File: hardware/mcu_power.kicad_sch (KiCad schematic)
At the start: 85 parts, among them Q201 MMBT3904, Q202 IRLML2244, SW201 Button Power, SW202 Reset, SW203 Button Enter, SW204 Button Left, SW205 Button Up, SW206 Button Down, SW207 Button Escape, SW208 Button Right, U201 STM32F405RGTx, U202 TPS7A2033, U203 TP6841S6, Y201 8 MHz

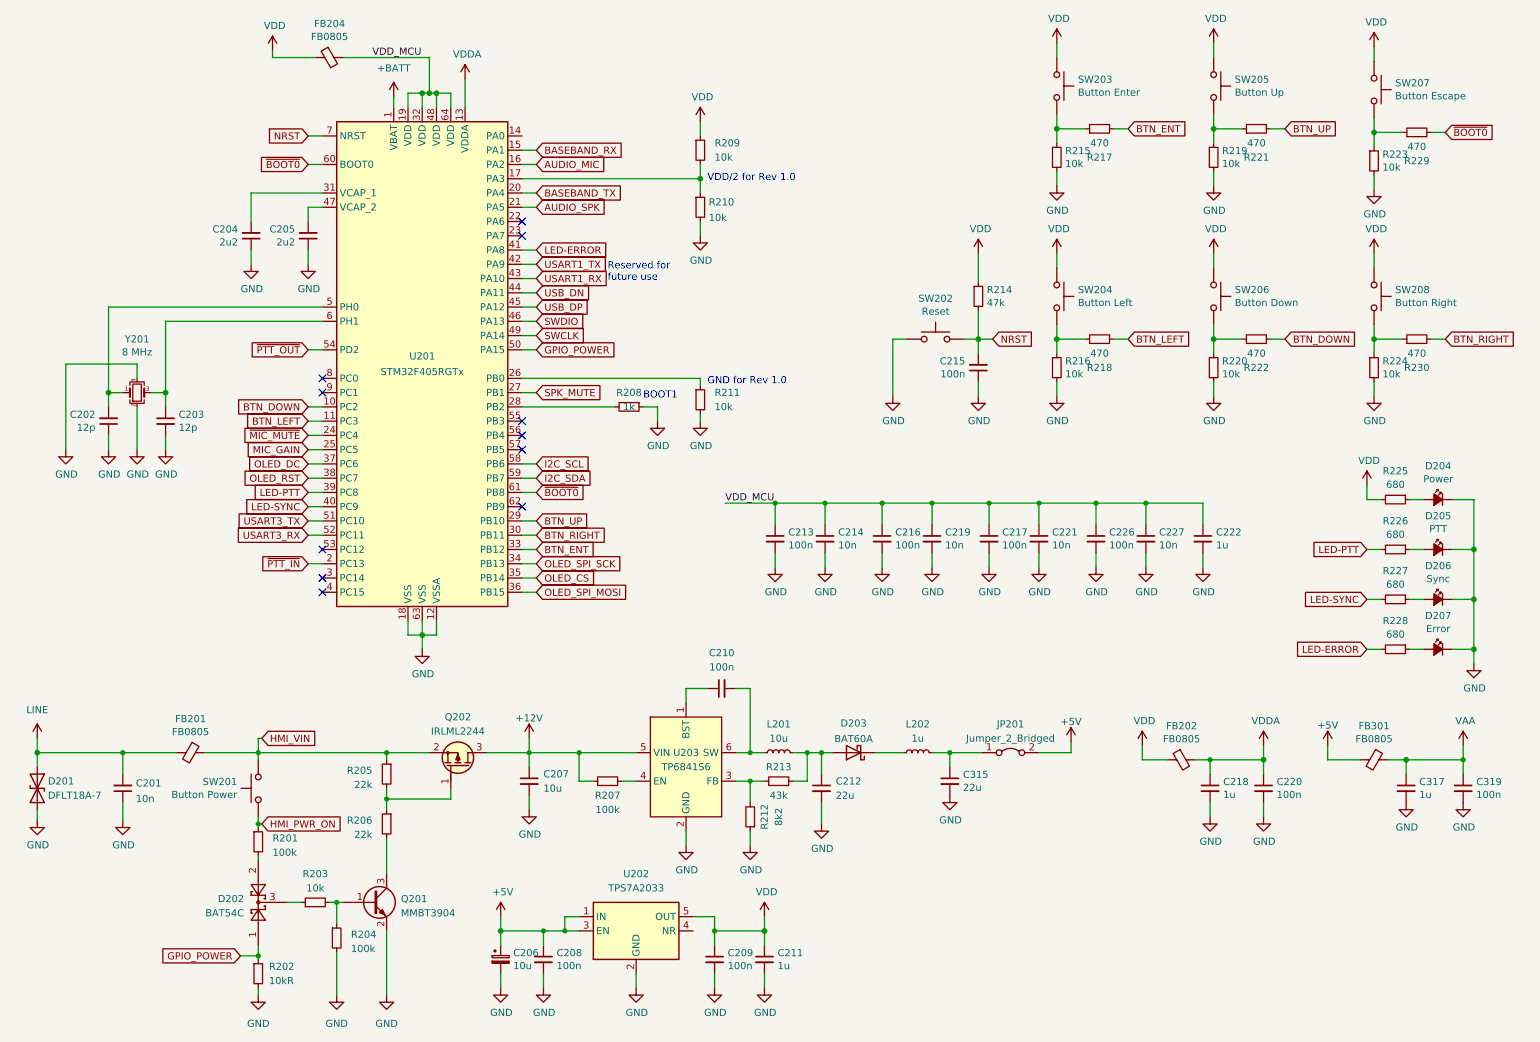
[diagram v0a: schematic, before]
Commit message: Updated various symbols attributes
Updated various components (mostly LEDs and switches) to simplify the BOM and make it more easily readable.
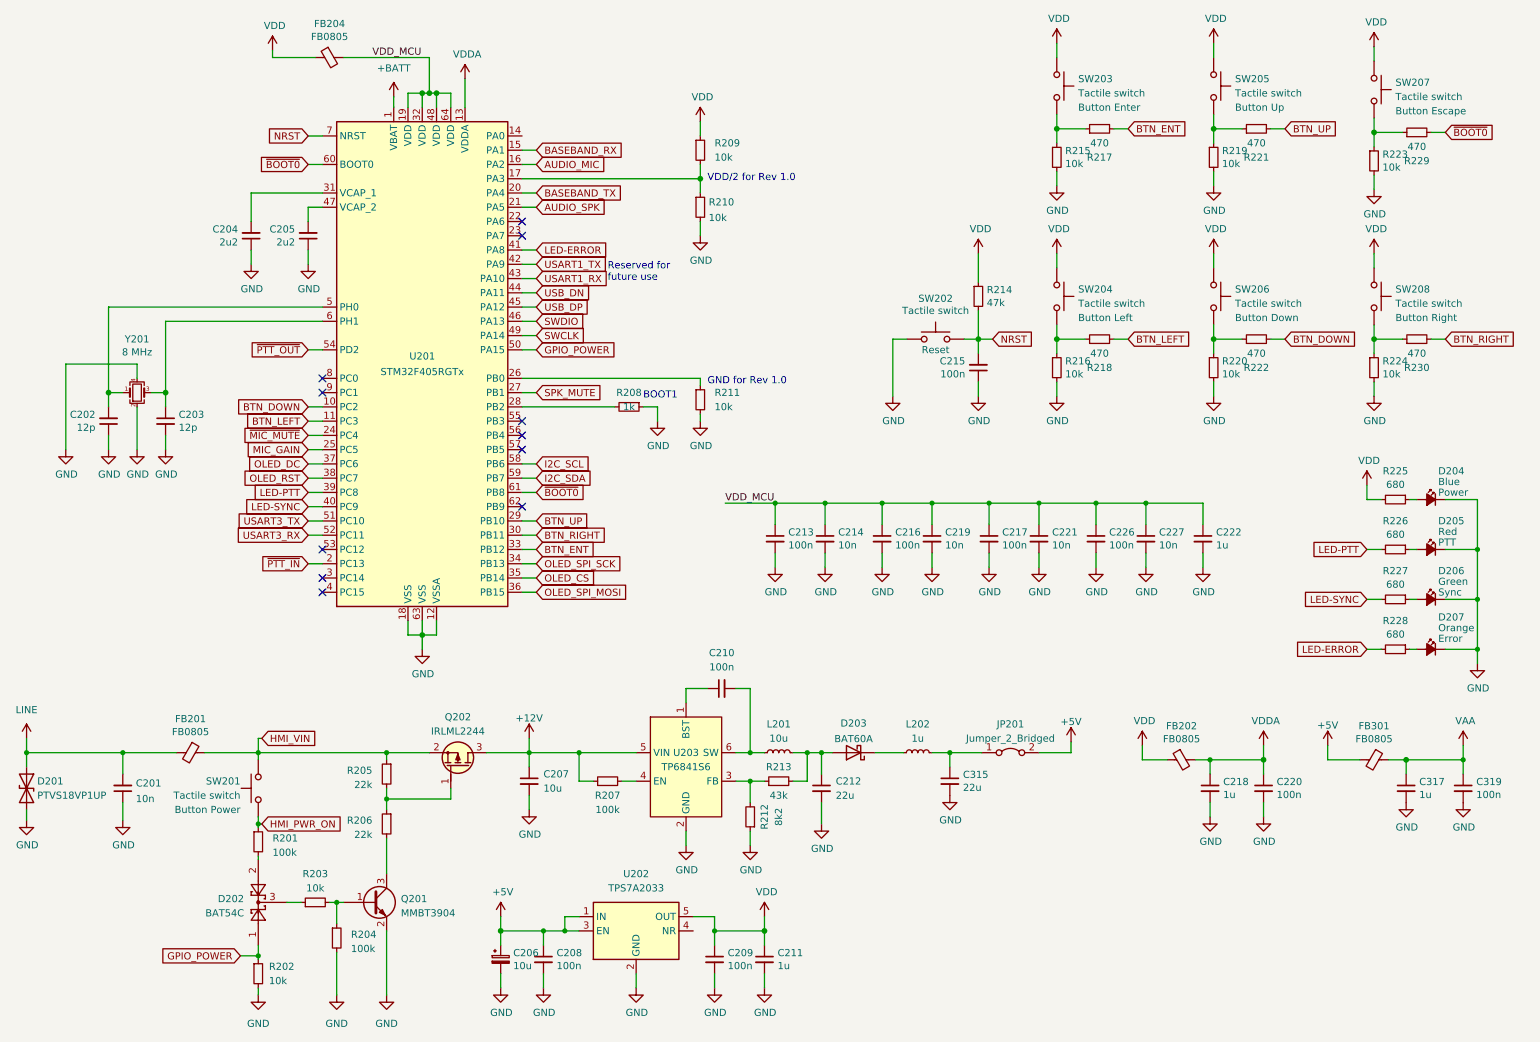
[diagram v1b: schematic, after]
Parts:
- D201: value DFLT18A-7 -> PTVS18VP1UP
- D204: value Power -> Blue; Comment (none) -> Power
- D205: value PTT -> Red; Comment (none) -> PTT
- D206: value Sync -> Green; Comment (none) -> Sync
- D207: value Error -> Orange; Comment (none) -> Error
- L202: LCSC Part # (none) -> C223144; MPN Generic L/1u/0805/1A -> Generic L/1u/0805/1A/<150mR
- R202: value 10kR -> 10k
- SW201: value Button Power -> Tactile switch; Alt LCSC Part # (none) -> C83916; Comment (none) -> Button Power; LCSC Part # C83916 -> C221869
- SW202: value Reset -> Tactile switch; Comment (none) -> Reset
- SW203: value Button Enter -> Tactile switch; Alt LCSC Part # (none) -> C83916; Comment (none) -> Button Enter; LCSC Part # C83916 -> C221869
- SW204: value Button Left -> Tactile switch; Alt LCSC Part # (none) -> C83916; Comment (none) -> Button Left; LCSC Part # C83916 -> C221869
- SW205: value Button Up -> Tactile switch; Alt LCSC Part # (none) -> C83916; Comment (none) -> Button Up; LCSC Part # C83916 -> C221869
- SW206: value Button Down -> Tactile switch; Alt LCSC Part # (none) -> C83916; Comment (none) -> Button Down; LCSC Part # C83916 -> C221869
- SW207: value Button Escape -> Tactile switch; Alt LCSC Part # (none) -> C83916; Comment (none) -> Button Escape; LCSC Part # C83916 -> C221869
- SW208: value Button Right -> Tactile switch; Alt LCSC Part # (none) -> C83916; Comment (none) -> Button Right; LCSC Part # C83916 -> C221869
- Y201: LCSC Part # C518156 -> C2442665
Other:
- moved on the sheet: D201, D204, D205, D206, D207

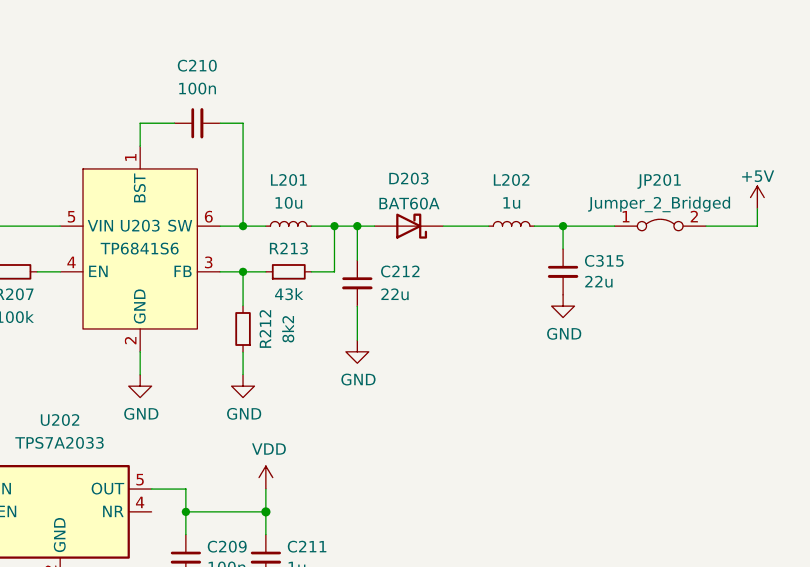
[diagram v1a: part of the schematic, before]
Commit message: Updated DC-DC output capacitor
Using 1206 footprint
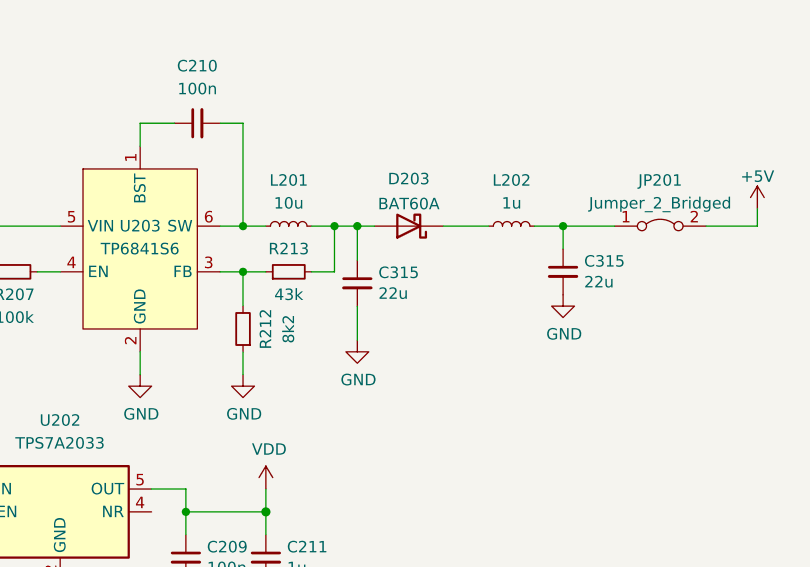
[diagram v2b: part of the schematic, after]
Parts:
- removed C212: 22u, Capacitor_SMD:C_1210_3225Metric, symbol Device:C_Small
- added C315: 22u, Capacitor_SMD:C_1206_3216Metric, symbol Device:C_Small
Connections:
- net GND: now also C315.2
- net at D203.2 (A), L201.1, R213.2: now also C315.1
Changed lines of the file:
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@@
   )
   (symbol (lib_id "Device:C_Small") (at 159.385 152.4 0) (unit 1)
-    (in_bom yes) (on_board yes) (dnp no) (fields_autoplaced)
-    (property "Reference" "C212" (at 161.925 151.1362 0)
+    (in_bom yes) (on_board yes) (dnp no)
+    (property "Reference" "C315" (at 161.7218 151.2316 0)
       (effects (font (size 1.27 1.27)) (justify left))
     )
-    (property "Value" "22u" (at 161.925 153.6762 0)
+    (property "Value" "22u" (at 161.7218 153.543 0)
       (effects (font (size 1.27 1.27)) (justify left))
     )
-    (property "Footprint" "Capacitor_SMD:C_1210_3225Metric" (at 159.385 152.4 0)
+    (property "Footprint" "Capacitor_SMD:C_1206_3216Metric" (at 159.385 152.4 0)
       (effects (font (size 1.524 1.524)) hide)
     )
@@
       (effects (font (size 1.524 1.524)))
     )
-    (property "MPN" "Generic C/22uF/C0G/10V/1210" (at 159.385 152.4 0)
+    (property "MPN" "Generic C/22uF/X7R/10V/1206" (at 159.385 152.4 0)
       (effects (font (size 1.27 1.27)) hide)
     )
@@
     (instances
       (project "M17-SmartMic"
+        (path "/59592280-3207-432b-a891-cd517ec5cf12/00000000-0000-0000-0000-0000612c969e"
+          (reference "C315") (unit 1)
+        )
         (path "/59592280-3207-432b-a891-cd517ec5cf12/00000000-0000-0000-0000-0000612c95ef"
           (reference "C212") (unit 1)
